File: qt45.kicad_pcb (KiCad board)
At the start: 2 copper layers, 266.7 x 81 mm, 106 parts, among them SW1 SW_PUSH, U1 ATmega32U4-AU, Y1 16MHz

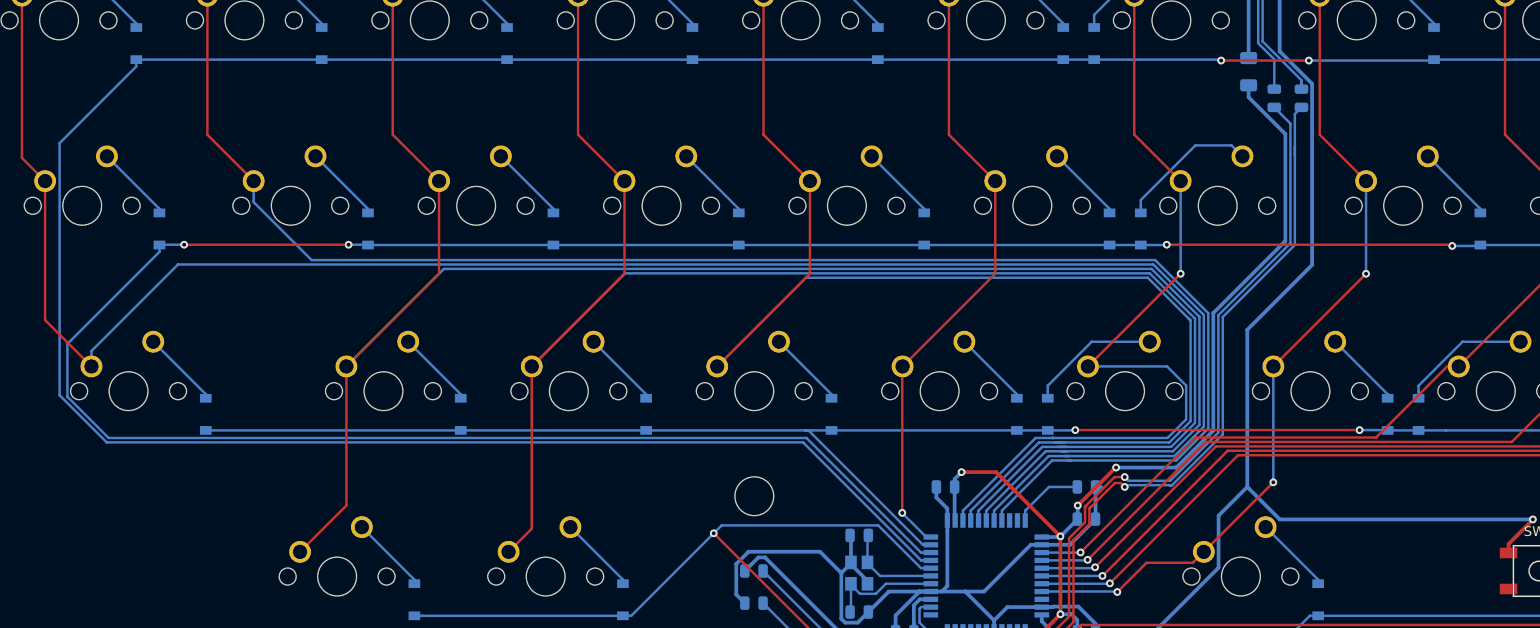
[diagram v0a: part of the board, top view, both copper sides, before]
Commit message: Re-route to maximise ground plane
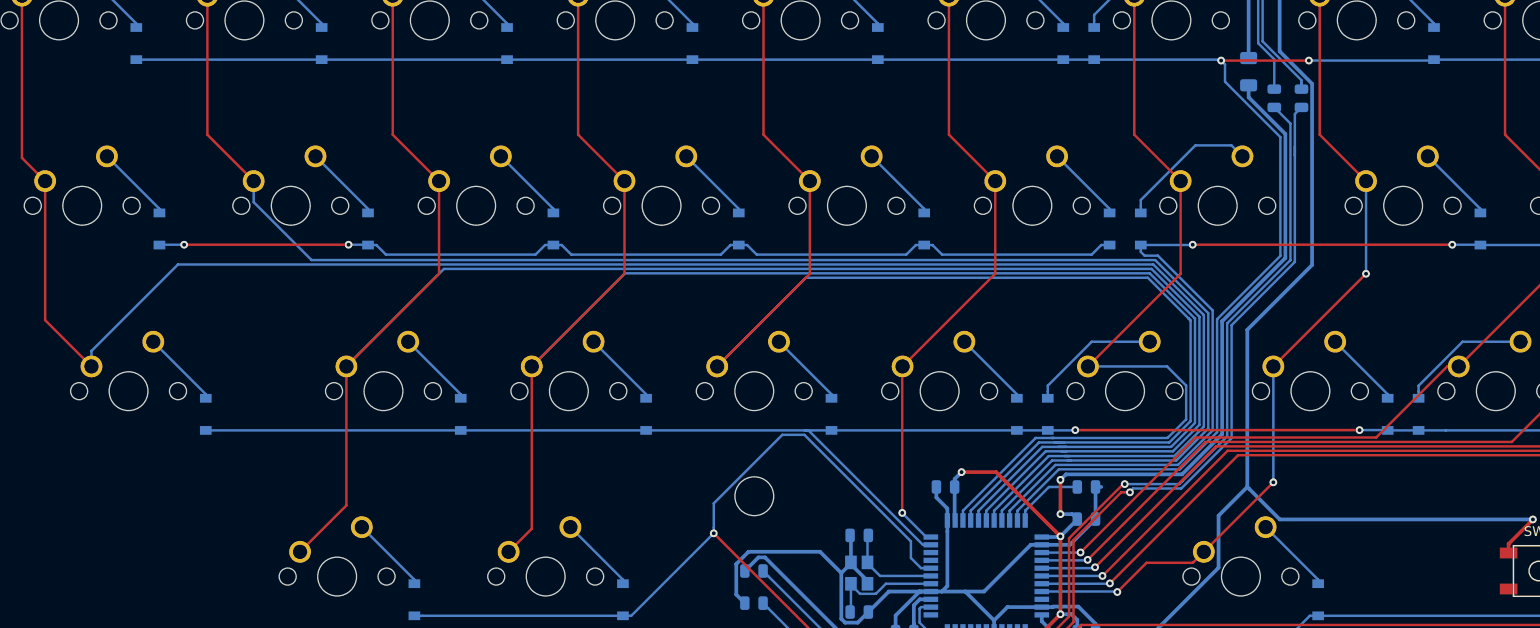
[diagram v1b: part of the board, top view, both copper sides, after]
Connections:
- U1 pad 19: ROW0 -> ROW2
- U1 pad 20: ROW1 -> Net-(U1-Pad20)
- U1 pad 21: ROW2 -> Net-(U1-Pad21)
- U1 pad 31: Net-(U1-Pad31) -> ROW1
- U1 pad 32: Net-(U1-Pad32) -> ROW0
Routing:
- net ROW1: track 353.1 -> 286.4 mm
- net ROW0: track 366.2 -> 300.1 mm
- net ROW3: track 221.1 -> 231.6 mm
- net +5V: track 149.0 -> 154.5 mm
- net Net-(R1-Pad1): track 76.5 -> 75.7 mm
- net Net-(R2-Pad1): track 78.9 -> 78.1 mm
- net COL6: vias 1 -> 0
